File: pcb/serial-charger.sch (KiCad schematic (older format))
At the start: 25 parts, among them IC1 CH340G, J1 jumper, J2 jumper, P1 CONN_01X02, P2 USB_OTG, P3 CONN_01X04, U1 XC6206, U2 FM6316FE, x1 xtal_osc

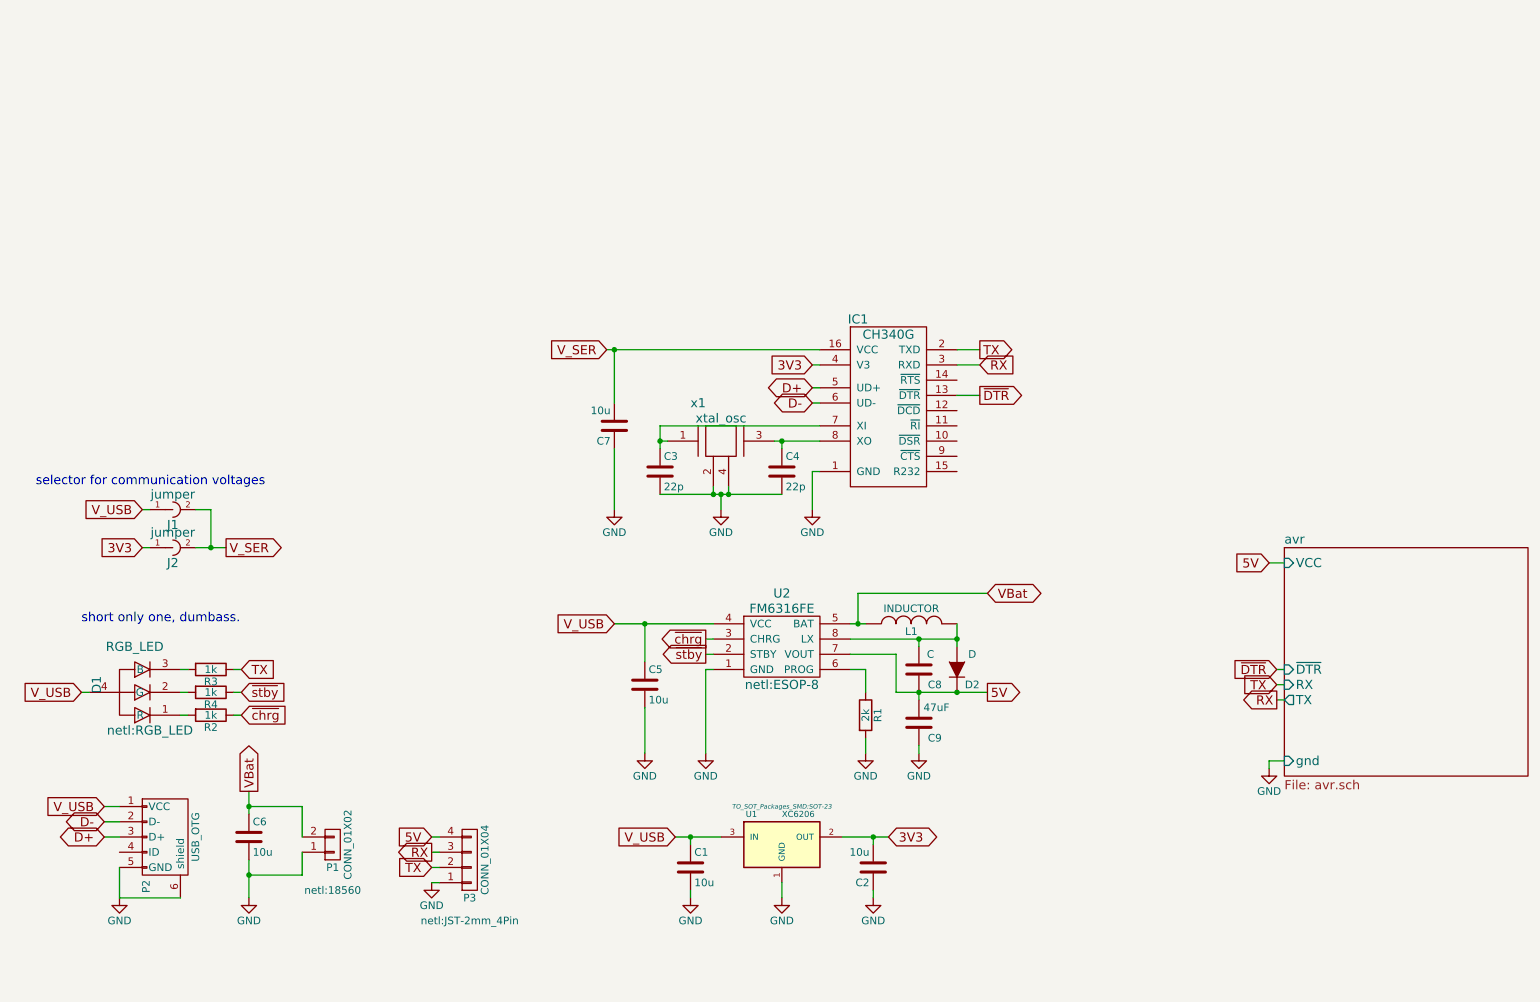
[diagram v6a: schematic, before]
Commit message: changed to hierarchial layout in schematics
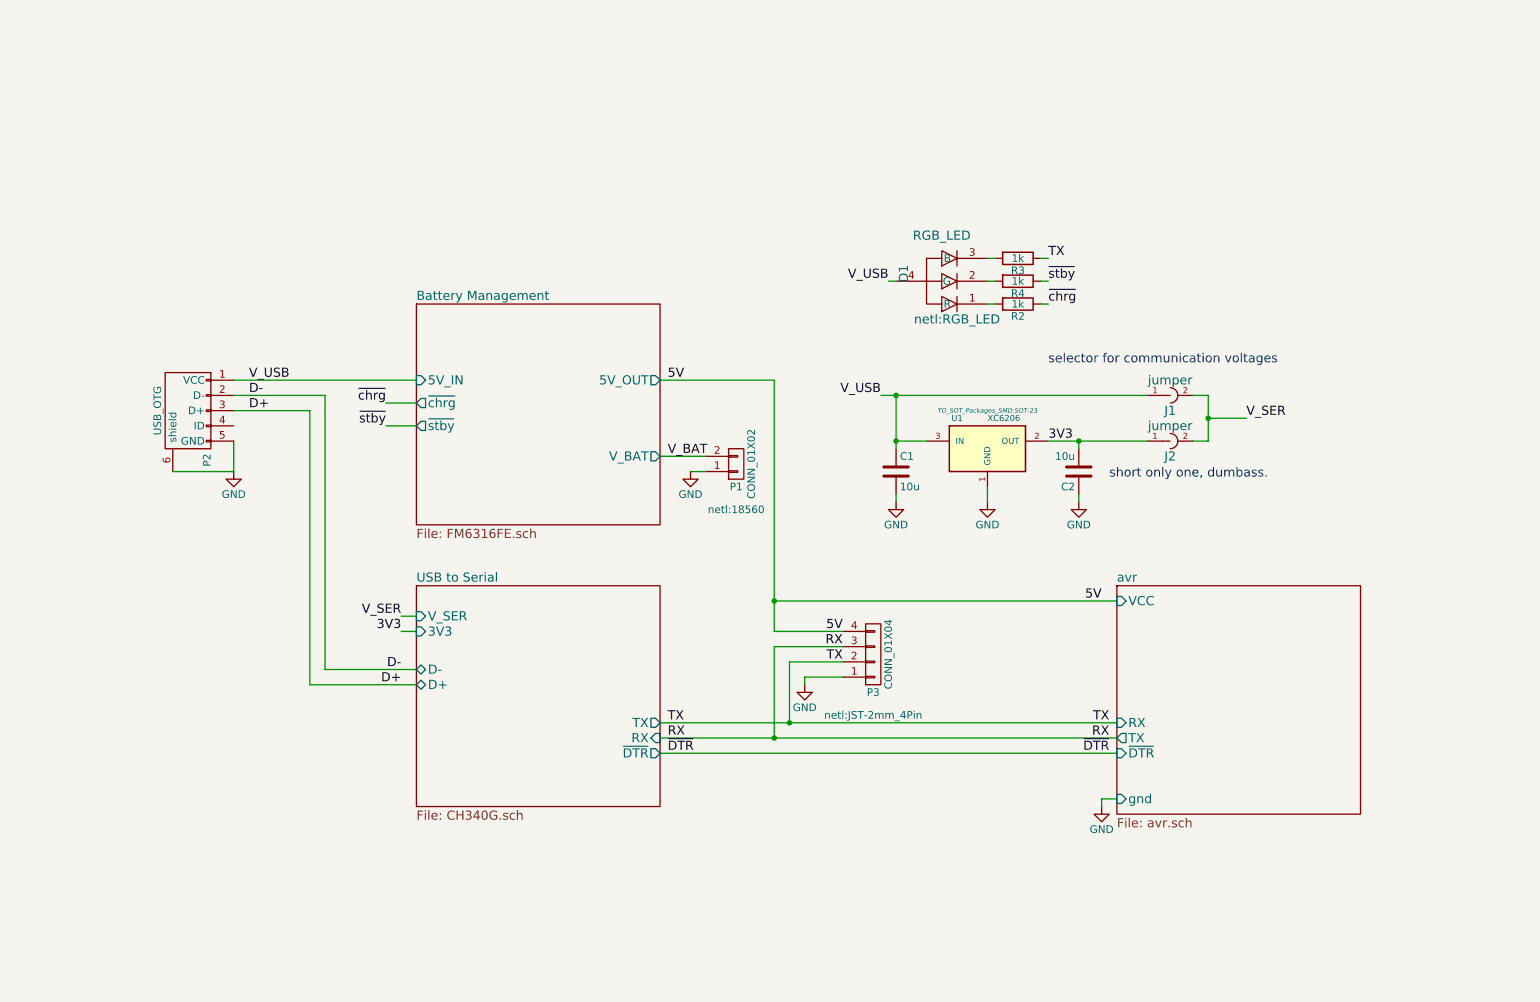
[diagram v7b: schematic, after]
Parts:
- removed C3, C4: 22p, netl:SMD_0603, symbol C
- removed C5, C6, C7: 10u, netl:SMD_0603, symbol C
- removed C8: C, netl:SMD_0603, symbol C
- removed C9: 47uF, netl:SMD_0603, symbol C
- removed D2: D, netl:SMD_0603, symbol D
- removed IC1: CH340G, Housings_SOIC:SOIC-16_3.9x9.9mm_Pitch1.27mm, symbol CH340G
- removed L1: INDUCTOR, netl:7x7_Inductor, symbol INDUCTOR
- removed R1: 2k, netl:SMD_0603, symbol R
- removed U2: FM6316FE, netl:ESOP-8, symbol FM6316FE
- removed x1: xtal_osc, netl:SM_3225, symbol xtal_osc
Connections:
- net VBat renamed V_BAT
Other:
- moved on the sheet: C1, C2, D1, J1, J2, P1, P2, P3, R2, R3, R4, U1
